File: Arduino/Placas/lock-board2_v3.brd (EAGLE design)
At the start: 11 parts

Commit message: lock board v3 modified
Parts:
- moved E$6 23.3 mm to (75.2, 81.3)
- moved E$11 23.3 mm to (75.0, 81.0)
- moved E$3 23.3 mm to (75.0, 33.0)
- moved E$1 23.3 mm to (74.7, 49.6)
- moved E$2 15.4 mm to (121.7, 75.3)
- moved 2 15.4 mm to (115.7, 58.2)
- moved 1 15.4 mm to (115.7, 64.2)
- moved E$4 15.0 mm to (150.0, 69.0)
- moved E$5 15.0 mm to (150.0, 60.0)
- moved E$7 15.0 mm to (150.2, 79.8)
- moved E$8 15.0 mm to (150.0, 51.0)
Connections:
- removed net S$2: 2.1, E$1.GND@1, E$4.1, E$5.1, E$7.1, E$8.1
- net S$1: now also E$6.14
- net S$3: now also 2.1, E$1.GND@1, E$4.1, E$5.1, E$7.1, E$8.1; no longer E$1.AD0, E$6.14
- net S$5: now also E$4.2
- net S$6: no longer E$5.2
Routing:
- net S$3: track 32.1 -> 243.4 mm
- net S$2: track 209.2 -> 0.00 mm
- net S$6: track 143.9 -> 0.00 mm
- net S$5: track 142.2 -> 254.6 mm
- net S$7: track 192.2 -> 287.9 mm
- net S$1: track 5.33 -> 74.0 mm
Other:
- board text added: "LCD"

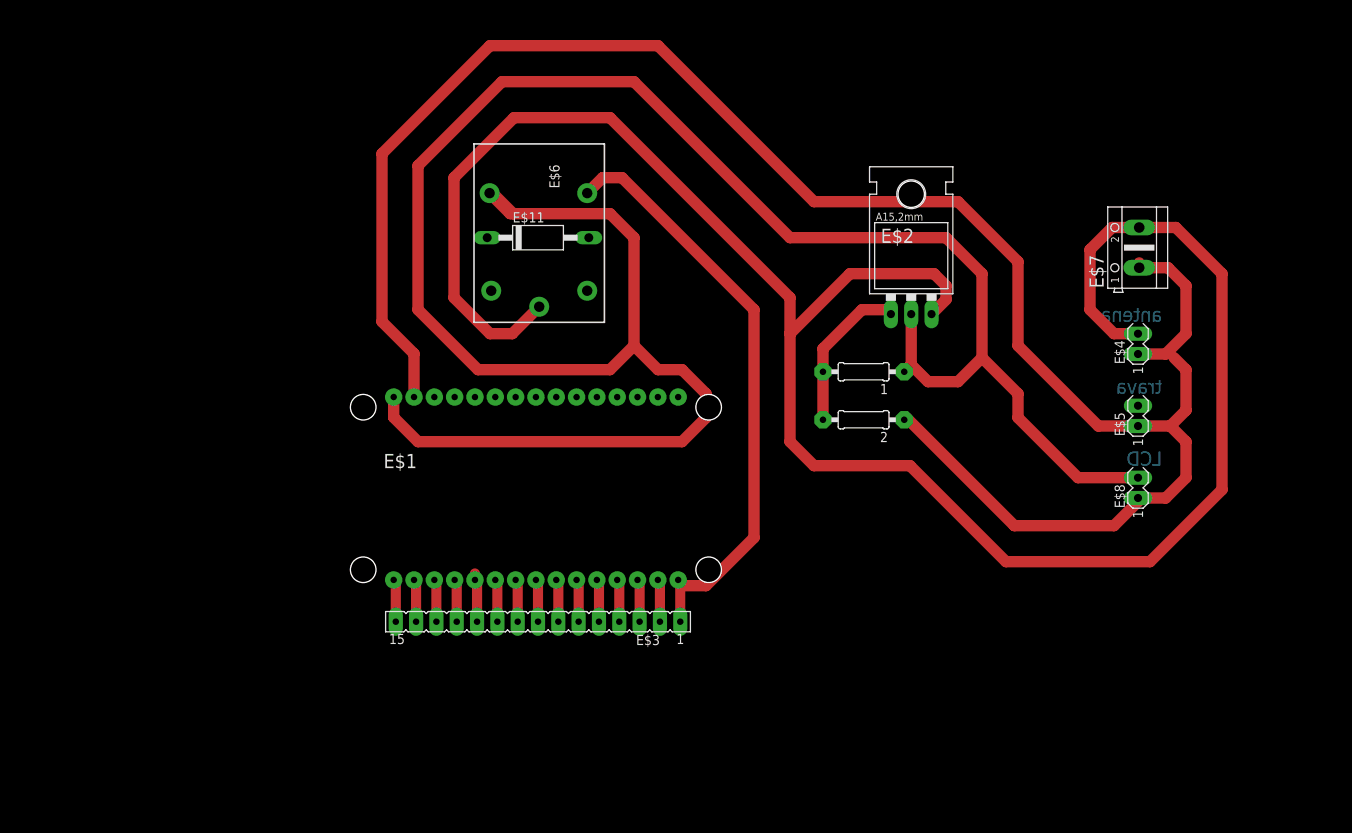
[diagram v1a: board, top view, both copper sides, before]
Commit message: board v3 created, not tested
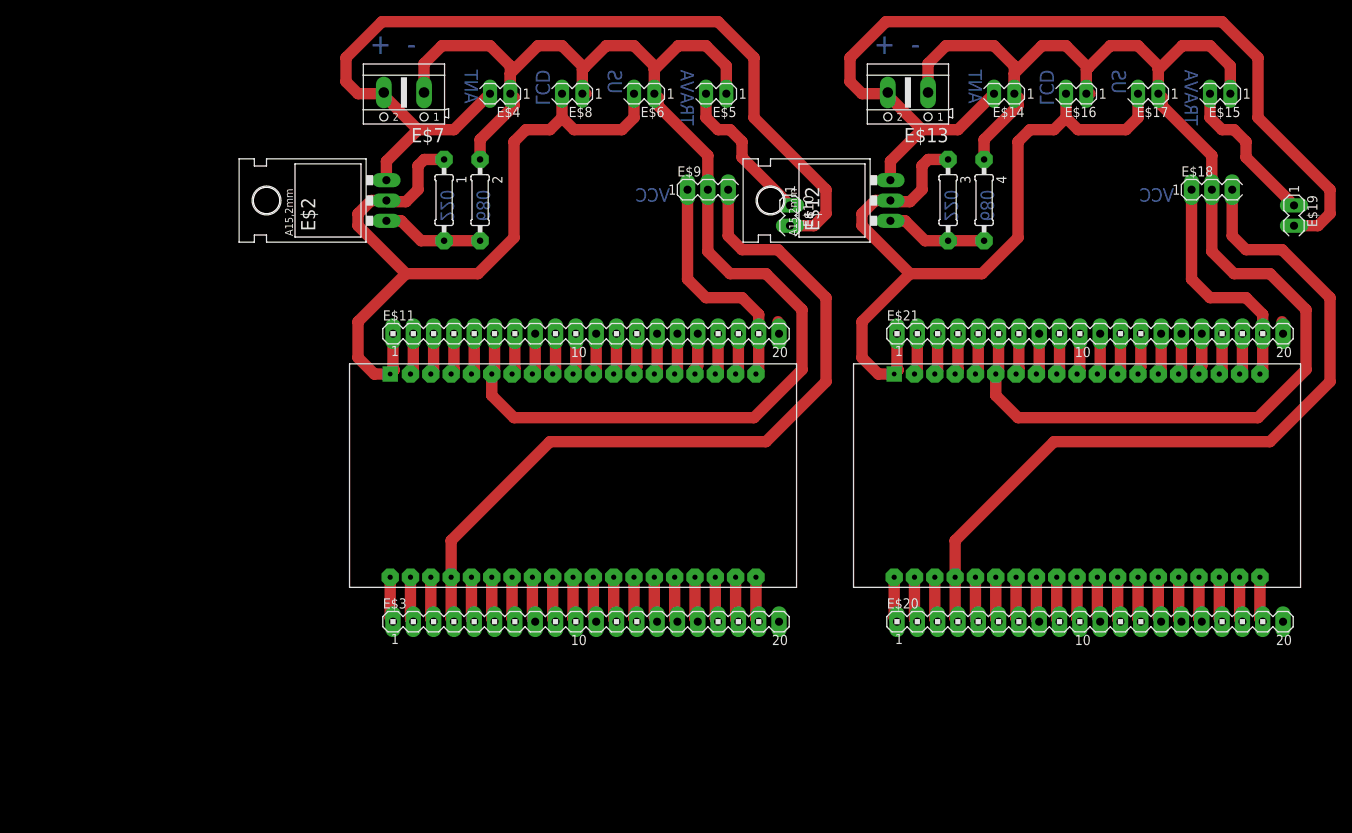
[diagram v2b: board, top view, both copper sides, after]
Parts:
- added 3, 4: (no value), eagle-ltspice:0207/10
- added E$10, E$14, E$15, E$16, E$17, E$19: (no value), con-lstb:MA03-1
- added E$12: (no value), v-reg:317TL
- added E$13: (no value), con-ptr500:AK500/2
- added E$18, E$9: (no value), con-lstb:MA04-1
- added E$20, E$21: (no value), con-lstb:MA20-1
- added E$22: (no value), esp32:ESP32
- E$1: device ESP12E_DEVKIT:ESP12E_DEVKIT -> esp32:ESP32
- E$11: device diode:P1-12E -> con-lstb:MA20-1
- E$3: device con-lsta:FE15 -> con-lstb:MA20-1
- E$6: device relay:ZN5 -> con-lstb:MA03-1
- moved E$7 93.9 mm to (58.2, 99.2), turned to 180 degrees
- moved E$8 86.5 mm to (78.0, 99.0), turned to 180 degrees
- moved E$4 86.4 mm to (69.0, 99.0), turned to 180 degrees
- moved E$2 70.2 mm to (52.2, 85.7), turned to 90 degrees
- moved E$5 66.6 mm to (96.0, 99.0), turned to 180 degrees
- moved 1 56.7 mm to (63.3, 85.7), turned to 270 degrees
- moved 2 55.2 mm to (67.8, 85.7), turned to 270 degrees
- moved E$1 48.2 mm to (87.0, 3.00)
- moved E$6 21.3 mm to (87.0, 99.0), turned to 180 degrees
- moved E$11 13.4 mm to (81.0, 69.0)
- moved E$3 6.00 mm to (81.0, 33.0), turned to 0 degrees
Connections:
- removed net S$6: E$6.A1
- new net S$10: E$1.P$73, E$3.4, E$9.3
- new net S$2: 2.1, E$1.P$44, E$11.6, E$4.1, E$5.1, E$6.1, E$7.1, E$8.1, E$9.2
- new net S$22: E$1.P$61, E$3.16
- new net S$23: E$1.P$60, E$3.17
- new net S$26: 1.1, E$1.P$20, E$11.1, E$2.2, E$6.2, E$8.2
- new net S$29: E$1.P$41, E$11.3
- new net S$30: E$1.P$42, E$11.4
- new net S$31: E$1.P$43, E$11.5
- new net S$32: E$11.20
- new net S$33: E$1.P$45, E$11.7
- new net S$34: E$1.P$46, E$11.8
- new net S$35: E$1.P$47, E$11.9
- new net S$36: E$1.P$48, E$11.10
- new net S$37: E$1.P$49, E$11.11
- new net S$38: E$1.P$50, E$11.12
- new net S$39: E$1.P$51, E$11.13
- new net S$40: E$1.P$52, E$11.14
- new net S$41: E$1.P$53, E$11.15
- new net S$42: E$1.P$54, E$11.16
- new net S$43: E$1.P$55, E$11.17
- new net S$44: E$1.P$56, E$11.18
- new net S$45: E$1.P$57, E$11.19, E$9.1
- new net S$46: E$12.3, E$13.2, E$14.2, E$19.2
- new net S$48: E$15.2, E$19.1
- new net S$49: E$20.1
- new net S$50: E$20.2
- new net S$51: E$20.3
- new net S$52: E$18.3, E$20.4
- new net S$53: E$20.5
- new net S$54: E$20.6
- new net S$55: E$20.7
- new net S$56: E$20.8
- new net S$57: E$20.9
- new net S$58: E$20.10
- new net S$59: E$20.11
- new net S$60: E$20.12
- new net S$61: E$20.13
- new net S$62: E$20.14
- new net S$63: E$20.15
- new net S$64: E$20.16
- new net S$65: E$20.17
- new net S$66: E$20.18
- new net S$67: E$20.19
- new net S$68: 3.1, E$12.2, E$16.2, E$17.2, E$21.1
- new net S$69: E$21.2
- new net S$70: E$21.3
- new net S$71: E$21.4
- new net S$72: E$21.5
- new net S$73: 4.1, E$13.1, E$14.1, E$15.1, E$16.1, E$17.1, E$18.2, E$21.6
- new net S$74: E$21.7
- new net S$75: E$21.8
- new net S$76: E$21.9
- new net S$77: E$21.10
- new net S$78: E$21.11
- new net S$79: E$21.12
- new net S$80: E$21.13
- new net S$81: E$21.14
- new net S$82: E$21.15
- new net S$83: E$21.16
- new net S$84: E$21.17
- new net S$85: E$21.18
- new net S$86: E$18.1, E$21.19
- new net S$87: E$21.20
- new net S$9: 3.2, 4.2, E$12.1
- net S$1: now also E$10.1, E$5.2; no longer E$1.D0, E$3.1, E$6.14
- net S$11: now also E$1.P$72, E$3.5; no longer E$1.D1, E$3.2
- net S$12: now also E$1.P$71, E$3.6; no longer E$1.D2, E$3.3
- net S$13: now also E$1.P$70, E$3.7; no longer E$1.D3, E$3.4
- net S$14: now also E$1.P$69, E$3.8; no longer E$1.D4, E$3.5
- net S$15: now also E$1.P$68, E$3.9; no longer E$1.3V3@1, E$3.6
- net S$16: now also E$1.P$67, E$3.10; no longer E$1.GND@2, E$3.7
- net S$17: now also E$1.P$66, E$3.11; no longer E$1.D5, E$3.8
- net S$18: now also E$1.P$65, E$3.12; no longer E$1.D6, E$3.9
- net S$19: now also E$1.P$64, E$3.13; no longer E$1.D7, E$3.10
- net S$20: now also E$1.P$63, E$3.14; no longer E$1.RX, E$3.12
- net S$21: now also E$1.P$62, E$3.15; no longer E$1.TX, E$3.13
- net S$24: now also E$1.P$59, E$3.18; no longer E$1.3V3@2, E$3.15
- net S$25: now also E$1.P$58, E$3.19; no longer E$1.GND@3, E$3.14
- net S$27: now also E$1.P$21, E$11.2; no longer E$6.A2
- net S$3: now also E$1.P$76, E$3.1; no longer 2.1, E$1.GND@1, E$4.1, E$5.1, E$7.1, E$8.1
- net S$4: now also E$1.P$75, E$3.2; no longer E$1.D8, E$3.11
- net S$5: now also E$10.2; no longer E$6.11
- net S$7: now also E$1.P$74, E$3.3; no longer 1.1, E$1.VIN, E$2.2, E$6.12, E$8.2
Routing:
- net S$7: track 287.9 -> 5.70 mm
- net S$3: track 243.4 -> 5.76 mm
- net S$73: track 0.00 -> 172.4 mm
- net S$2: track 0.00 -> 172.4 mm
- net S$5: track 254.6 -> 116.7 mm
- net S$46: track 0.00 -> 116.7 mm
- net S$26: track 0.00 -> 99.4 mm
- net S$68: track 0.00 -> 99.4 mm
- net S$52: track 0.00 -> 97.1 mm
- net S$10: track 0.00 -> 97.1 mm
- net S$1: track 74.0 -> 19.2 mm
- net S$45: track 0.00 -> 29.5 mm
- net S$86: track 0.00 -> 29.5 mm
- net S$48: track 0.00 -> 19.2 mm
- net S$9: track 0.00 -> 12.7 mm
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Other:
- board text added: "- +"
- board text added: "220"
- board text added: "680"
- board text added: "ANT"
- board text added: "TRAVA"
- board text added: "US"
- board text added: "VCC"
- board text removed: "antena"
- board text removed: "trava"

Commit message: V3 lock board finished
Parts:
- removed 1, 2: (no value), eagle-ltspice:0207/10
- removed E$1: (no value), esp32:ESP32
- removed E$10, E$4, E$5, E$6, E$8: (no value), con-lstb:MA03-1
- removed E$11, E$3: (no value), con-lstb:MA20-1
- removed E$2: (no value), v-reg:317TL
- removed E$7: (no value), con-ptr500:AK500/2
- removed E$9: (no value), con-lstb:MA04-1
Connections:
- removed net S$1: E$10.1, E$5.2
- removed net S$10: E$1.P$73, E$3.4, E$9.3
- removed net S$11: E$1.P$72, E$3.5
- removed net S$12: E$1.P$71, E$3.6
- removed net S$13: E$1.P$70, E$3.7
- removed net S$14: E$1.P$69, E$3.8
- removed net S$15: E$1.P$68, E$3.9
- removed net S$16: E$1.P$67, E$3.10
- removed net S$17: E$1.P$66, E$3.11
- removed net S$18: E$1.P$65, E$3.12
- removed net S$19: E$1.P$64, E$3.13
- removed net S$2: 2.1, E$1.P$44, E$11.6, E$4.1, E$5.1, E$6.1, E$7.1, E$8.1, E$9.2
- removed net S$20: E$1.P$63, E$3.14
- removed net S$21: E$1.P$62, E$3.15
- removed net S$22: E$1.P$61, E$3.16
- removed net S$23: E$1.P$60, E$3.17
- removed net S$24: E$1.P$59, E$3.18
- removed net S$25: E$1.P$58, E$3.19
- removed net S$26: 1.1, E$1.P$20, E$11.1, E$2.2, E$6.2, E$8.2
- removed net S$27: E$1.P$21, E$11.2
- removed net S$29: E$1.P$41, E$11.3
- removed net S$3: E$1.P$76, E$3.1
- removed net S$30: E$1.P$42, E$11.4
- removed net S$31: E$1.P$43, E$11.5
- removed net S$32: E$11.20
- removed net S$33: E$1.P$45, E$11.7
- removed net S$34: E$1.P$46, E$11.8
- removed net S$35: E$1.P$47, E$11.9
- removed net S$36: E$1.P$48, E$11.10
- removed net S$37: E$1.P$49, E$11.11
- removed net S$38: E$1.P$50, E$11.12
- removed net S$39: E$1.P$51, E$11.13
- removed net S$4: E$1.P$75, E$3.2
- removed net S$40: E$1.P$52, E$11.14
- removed net S$41: E$1.P$53, E$11.15
- removed net S$42: E$1.P$54, E$11.16
- removed net S$43: E$1.P$55, E$11.17
- removed net S$44: E$1.P$56, E$11.18
- removed net S$45: E$1.P$57, E$11.19, E$9.1
- removed net S$5: E$10.2, E$2.3, E$4.2, E$7.2
- removed net S$7: E$1.P$74, E$3.3
- removed net S$8: 1.2, 2.2, E$2.1
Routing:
- net S$2: track 172.4 -> 0.00 mm
- net S$5: track 116.7 -> 0.00 mm
- net S$26: track 99.4 -> 0.00 mm
- net S$10: track 97.1 -> 0.00 mm
- net S$45: track 29.5 -> 0.00 mm
- net S$1: track 19.2 -> 0.00 mm
- net S$8: track 12.7 -> 0.00 mm
- net S$17: track 5.80 -> 0.00 mm
- net S$3: track 5.76 -> 0.00 mm
- net S$20: track 5.75 -> 0.00 mm
- net S$25: track 5.70 -> 0.00 mm
- net S$23: track 5.70 -> 0.00 mm
- net S$21: track 5.70 -> 0.00 mm
- net S$18: track 5.70 -> 0.00 mm
- net S$16: track 5.70 -> 0.00 mm
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
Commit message: Small changes in board
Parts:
- removed 3, 4: (no value), eagle-ltspice:0207/10
- removed E$12: (no value), v-reg:317TL
- removed E$13: (no value), con-ptr500:AK500/2
- removed E$14, E$15, E$16, E$17, E$19: (no value), con-lstb:MA03-1
- removed E$18: (no value), con-lstb:MA04-1
- removed E$20, E$21: (no value), con-lstb:MA20-1
- removed E$22: (no value), esp32:ESP32
- added 1, 2: (no value), eagle-ltspice:0207/10
- added E$1: (no value), v-reg:317TL
- added E$10, E$9: (no value), con-lstb:MA20-1
- added E$11, E$3, E$4, E$5, E$6, E$8: (no value), con-lstb:MA03-1
- added E$2: (no value), con-ptr500:AK500/2
- added E$23: (no value), esp32:ESP32
- added E$7: (no value), con-lstb:MA04-1
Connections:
- removed net S$46: E$12.3, E$13.2, E$14.2, E$19.2
- removed net S$48: E$15.2, E$19.1
- removed net S$49: E$20.1
- removed net S$50: E$20.2
- removed net S$51: E$20.3
- removed net S$52: E$18.3, E$20.4
- removed net S$53: E$20.5
- removed net S$54: E$20.6
- removed net S$55: E$20.7
- removed net S$56: E$20.8
- removed net S$57: E$20.9
- removed net S$58: E$20.10
- removed net S$59: E$20.11
- removed net S$60: E$20.12
- removed net S$61: E$20.13
- removed net S$62: E$20.14
- removed net S$63: E$20.15
- removed net S$64: E$20.16
- removed net S$65: E$20.17
- removed net S$66: E$20.18
- removed net S$67: E$20.19
- removed net S$68: 3.1, E$12.2, E$16.2, E$17.2, E$21.1
- removed net S$69: E$21.2
- removed net S$70: E$21.3
- removed net S$71: E$21.4
- removed net S$72: E$21.5
- removed net S$73: 4.1, E$13.1, E$14.1, E$15.1, E$16.1, E$17.1, E$18.2, E$21.6
- removed net S$74: E$21.7
- removed net S$75: E$21.8
- removed net S$76: E$21.9
- removed net S$77: E$21.10
- removed net S$78: E$21.11
- removed net S$79: E$21.12
- removed net S$80: E$21.13
- removed net S$81: E$21.14
- removed net S$82: E$21.15
- removed net S$83: E$21.16
- removed net S$84: E$21.17
- removed net S$85: E$21.18
- removed net S$86: E$18.1, E$21.19
- removed net S$87: E$21.20
- removed net S$9: 3.2, 4.2, E$12.1
- new net S$1: 1.2, 2.2, E$1.1
- new net S$10: E$9.3
- new net S$100: E$9.19
- new net S$101: 1.1, E$1.2, E$10.1, E$5.2, E$6.2
- new net S$102: E$10.2
- new net S$103: E$10.3
- new net S$104: E$10.4
- new net S$105: E$10.5
- new net S$106: 2.1, E$10.6, E$11.1, E$2.1, E$3.1, E$4.1, E$5.1, E$6.1, E$7.2
- new net S$107: E$10.7
- new net S$108: E$10.8
- new net S$109: E$10.9
- new net S$110: E$10.10
- new net S$111: E$10.11
- new net S$112: E$10.12
- new net S$113: E$10.13
- new net S$114: E$10.14
- new net S$115: E$10.15
- new net S$116: E$10.16
- new net S$117: E$10.17
- new net S$118: E$10.18
- new net S$119: E$10.19, E$7.1
- new net S$120: E$10.20
- new net S$2: E$1.3, E$11.2, E$2.2, E$3.2, E$8.2
- new net S$26: E$7.3, E$9.4
- new net S$32: E$9.5
- new net S$45: E$9.6
- new net S$5: E$4.2, E$8.1
- new net S$6: E$9.1
- new net S$8: E$9.2
- new net S$88: E$9.7
- new net S$89: E$9.8
- new net S$90: E$9.9
- new net S$91: E$9.10
- new net S$92: E$9.11
- new net S$93: E$9.12
- new net S$94: E$9.13
- new net S$95: E$9.14
- new net S$96: E$9.15
- new net S$97: E$9.16
- new net S$98: E$9.17
- new net S$99: E$9.18
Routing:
- net S$106: track 0.00 -> 192.9 mm
- net S$73: track 172.4 -> 0.00 mm
- net S$2: track 0.00 -> 134.8 mm
- net S$46: track 116.7 -> 0.00 mm
- net S$101: track 0.00 -> 101.9 mm
- net S$68: track 99.4 -> 0.00 mm
- net S$26: track 0.00 -> 97.1 mm
- net S$52: track 97.1 -> 0.00 mm
- net S$119: track 0.00 -> 29.5 mm
- net S$86: track 29.5 -> 0.00 mm
- net S$48: track 19.2 -> 0.00 mm
- net S$5: track 0.00 -> 16.6 mm
- net S$1: track 0.00 -> 12.7 mm
- net S$9: track 12.7 -> 0.00 mm
- net S$59: track 5.80 -> 0.00 mm
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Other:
- board text added: "ANT1"
- board text added: "ANT2"
- board text removed: "ANT"
